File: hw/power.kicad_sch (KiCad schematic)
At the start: 46 parts, among them J9 Expansion, Q8 DMC2053UVT, U1 RT8096B, U2 RT8096B, U3 RT8096B, U5 TPS563249DDC

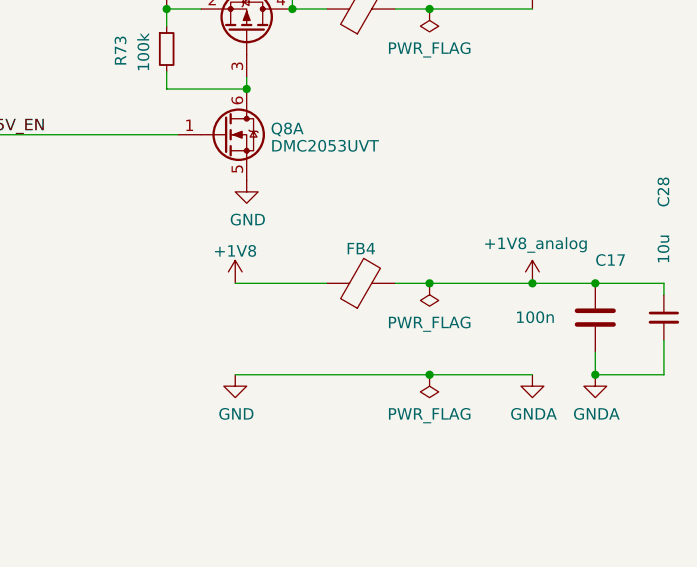
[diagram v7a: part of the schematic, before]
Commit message: rewired 1V8_analog to +2V5_analog
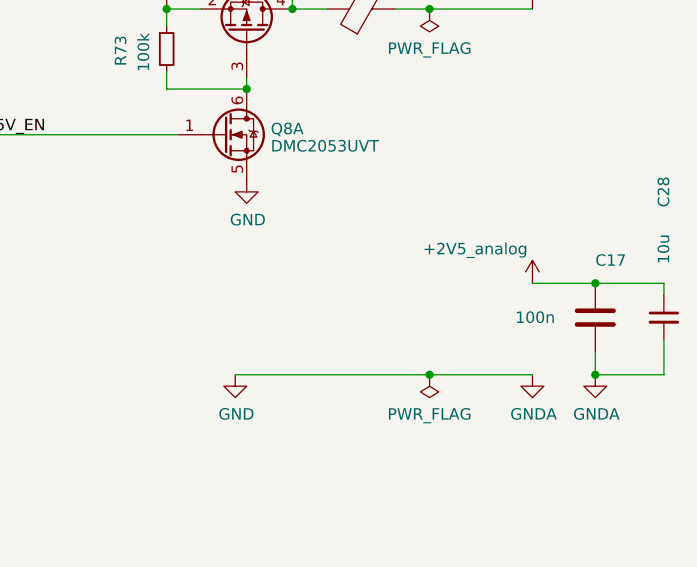
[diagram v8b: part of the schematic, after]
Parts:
- removed FB4: Ferrite_Bead MPZ1608S221A, Inductor_SMD:L_0603_1608Metric, symbol Device:FerriteBead
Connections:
- net +1V8_analog is gone; now on net +2V5_analog: C17.2, C28.1
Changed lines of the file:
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@@
   (junction (at 81.28 81.28) (diameter 0) (color 0 0 0 0)
   )
-  (junction (at 252.73 88.9) (diameter 0) (color 0 0 0 0)
-  )
   (junction (at 81.28 43.18) (diameter 0) (color 0 0 0 0)
   )
@@
   (junction (at 60.96 57.15) (diameter 0) (color 0 0 0 0)
   )
-  (junction (at 241.3 88.9) (diameter 0) (color 0 0 0 0)
-  )
   (junction (at 54.61 106.68) (diameter 0) (color 0 0 0 0)
   )
@@
     (stroke (width 0) (type default))
   )
-  (wire (pts (xy 237.49 88.9) (xy 241.3 88.9))
-    (stroke (width 0) (type default))
-  )
   (wire (pts (xy 119.38 138.43) (xy 128.27 138.43))
     (stroke (width 0) (type default))
@@
     (stroke (width 0) (type default))
   )
-  (wire (pts (xy 241.3 88.9) (xy 252.73 88.9))
-    (stroke (width 0) (type default))
-  )
   (wire (pts (xy 99.06 69.85) (xy 99.06 72.39))
     (stroke (width 0) (type default))
@@
   )
   (wire (pts (xy 92.71 72.39) (xy 93.98 72.39))
-    (stroke (width 0) (type default))
-  )
-  (wire (pts (xy 219.71 88.9) (xy 229.87 88.9))
     (stroke (width 0) (type default))
   )
@@
     )
   )
-  (symbol (lib_id "fmc:+1V8_analog") (at 252.73 88.9 0) (unit 1)
-    (in_bom yes) (on_board yes) (dnp no)
-    (property "Reference" "#PWR0168" (at 252.73 92.71 0)
-      (effects (font (size 1.27 1.27)) hide)
-    )
-    (property "Value" "+1V8_analog" (at 253.111 84.5058 0)
-      (effects (font (size 1.27 1.27)))
-    )
-    (property "Footprint" "" (at 252.73 88.9 0)
-      (effects (font (size 1.27 1.27)) hide)
-    )
-    (property "Datasheet" "" (at 252.73 88.9 0)
-      (effects (font (size 1.27 1.27)) hide)
-    )
-    (pin "1")
-    (instances
-      (project "usbadc"
-        (path "/7c8a1f8d-8834-4c9b-aaae-1f231e9b09a1/00000000-0000-0000-0000-00006086f2e3"
-          (reference "#PWR0168") (unit 1)
-        )
-      )
-    )
-  )
   (symbol (lib_id "fmc:+2V5_analog") (at 124.46 105.41 0) (unit 1)
     (in_bom yes) (on_board yes) (dnp no)
@@
     )
   )
-  (symbol (lib_id "Device:FerriteBead") (at 233.68 88.9 90) (unit 1)
-    (in_bom yes) (on_board yes) (dnp no)
-    (property "Reference" "FB4" (at 233.68 85.09 90)
-      (effects (font (size 1.27 1.27)))
-    )
-    (property "Value" "Ferrite_Bead MPZ1608S221A" (at 233.68 95.25 90)
-      (effects (font (size 1.27 1.27)) hide)
-    )
-    (property "Footprint" "Inductor_SMD:L_0603_1608Metric" (at 233.68 90.678 90)
-      (effects (font (size 1.27 1.27)) hide)
-    )
-    (property "Datasheet" "~" (at 233.68 88.9 0)
-      (effects (font (size 1.27 1.27)) hide)
-    )
-    (property "Part" "MPZ1608S221ATA00" (at 233.68 88.9 90)
-      (effects (font (size 1.27 1.27)) hide)
-    )
-    (property "Manufacturer" "TDK" (at 233.68 88.9 90)
-      (effects (font (size 1.27 1.27)) hide)
-    )
-    (pin "1")
-    (pin "2")
-    (instances
-      (project "usbadc"
-        (path "/7c8a1f8d-8834-4c9b-aaae-1f231e9b09a1/00000000-0000-0000-0000-00006086f2e3"
-          (reference "FB4") (unit 1)
-        )
-      )
-    )
-  )
-  (symbol (lib_id "power:+1V8") (at 219.71 88.9 0) (unit 1)
-    (in_bom yes) (on_board yes) (dnp no)
-    (property "Reference" "#PWR0166" (at 219.71 92.71 0)
-      (effects (font (size 1.27 1.27)) hide)
-    )
-    (property "Value" "+1V8" (at 219.71 85.344 0)
-      (effects (font (size 1.27 1.27)))
-    )
-    (property "Footprint" "" (at 219.71 88.9 0)
-      (effects (font (size 1.27 1.27)) hide)
-    )
-    (property "Datasheet" "" (at 219.71 88.9 0)
-      (effects (font (size 1.27 1.27)) hide)
-    )
-    (pin "1")
-    (instances
-      (project "usbadc"
-        (path "/7c8a1f8d-8834-4c9b-aaae-1f231e9b09a1/00000000-0000-0000-0000-00006086f2e3"
-          (reference "#PWR0166") (unit 1)
-        )
-      )
-    )
-  )
   (symbol (lib_id "power:+5V") (at 212.09 58.42 0) (unit 1)
     (in_bom yes) (on_board yes) (dnp no)
@@
         (path "/7c8a1f8d-8834-4c9b-aaae-1f231e9b09a1/00000000-0000-0000-0000-00006086f2e3"
           (reference "#FLG0106") (unit 1)
-        )
-      )
-    )
-  )
-  (symbol (lib_id "power:PWR_FLAG") (at 241.3 88.9 0) (mirror x) (unit 1)
-    (in_bom yes) (on_board yes) (dnp no)
-    (property "Reference" "#FLG0108" (at 241.3 90.805 0)
-      (effects (font (size 1.27 1.27)) hide)
-    )
-    (property "Value" "PWR_FLAG" (at 241.3 93.2942 0)
-      (effects (font (size 1.27 1.27)))
-    )
-    (property "Footprint" "" (at 241.3 88.9 0)
-      (effects (font (size 1.27 1.27)) hide)
-    )
-    (property "Datasheet" "~" (at 241.3 88.9 0)
-      (effects (font (size 1.27 1.27)) hide)
-    )
-    (pin "1")
-    (instances
-      (project "usbadc"
-        (path "/7c8a1f8d-8834-4c9b-aaae-1f231e9b09a1/00000000-0000-0000-0000-00006086f2e3"
-          (reference "#FLG0108") (unit 1)
         )
       )
@@
         )
       )
+    )
+  )
+  (symbol (lib_id "fmc:+2V5_analog") (at 252.73 88.9 0) (mirror y) (unit 1)
+    (in_bom yes) (on_board yes) (dnp no)
+    (property "Reference" "#PWR093" (at 252.73 92.71 0)
+      (effects (font (size 1.27 1.27)) hide)
+    )
+    (property "Value" "+2V5_analog" (at 246.38 85.09 0)
+      (effects (font (size 1.27 1.27)))
+    )
+    (property "Footprint" "" (at 252.73 88.9 0)
+      (effects (font (size 1.27 1.27)) hide)
+    )
+    (property "Datasheet" "" (at 252.73 88.9 0)
+      (effects (font (size 1.27 1.27)) hide)
+    )
+    (pin "1")
+    (instances
+      (project "usbadc"
+        (path "/7c8a1f8d-8834-4c9b-aaae-1f231e9b09a1/00000000-0000-0000-0000-00006086f2e3"
+          (reference "#PWR093") (unit 1)
+        )
+      )
